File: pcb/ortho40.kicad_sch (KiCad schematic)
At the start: 129 parts, among them J1 SWD, J2 USB_C_Receptacle_USB2.0, SW1 SW_Push, U1 RP2040, U2 XC6206PxxxMR, U3 W25Q128JVS, U4 USBLC6-2SC6, U5 ST7735S_1.8inch, Y1 12MHz

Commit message: Fully finish PCB
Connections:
- net c0: now also U1.34 (GPIO22)
- net c1: now also U1.35 (GPIO23)
- net c10: now also U1.6 (GPIO4)
- net c11: now also U1.7 (GPIO5)
- net c2: now also U1.36 (GPIO24)
- net c3: now also U1.37 (GPIO25)
- net c4: now also U1.38 (GPIO26/ADC0)
- net c5: now also U1.39 (GPIO27/ADC1)
- net c6: now also U1.2 (GPIO0)
- net c7: now also U1.3 (GPIO1)
- net c8: now also U1.4 (GPIO2)
- net c9: now also U1.5 (GPIO3)
- net r0: now also U1.41 (GPIO29/ADC3)
- net r1: now also U1.40 (GPIO28/ADC2)
- net r2: now also U1.13 (GPIO10)
- net r3: now also U1.14 (GPIO11)
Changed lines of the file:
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@@
     (effects (font (size 1.27 1.27) italic) (justify left bottom))
   )
+  (global_label "c4" (shape input) (at 76.708 100.584 0) (fields_autoplaced)
+    (effects (font (size 1.27 1.27)) (justify left))
+    (property "Intersheet References" "${INTERSHEET_REFS}" (id 0) (at 81.4192 100.5046 0)
+      (effects (font (size 1.27 1.27)) (justify left) hide)
+    )
+  )
   (global_label "LCD_RESET" (shape input) (at 43.942 168.91 180) (fields_autoplaced)
     (effects (font (size 1.27 1.27)) (justify right))
@@
     )
   )
+  (global_label "c11" (shape input) (at 76.708 43.434 0) (fields_autoplaced)
+    (effects (font (size 1.27 1.27)) (justify left))
+    (property "Intersheet References" "${INTERSHEET_REFS}" (id 0) (at 82.6287 43.3546 0)
+      (effects (font (size 1.27 1.27)) (justify left) hide)
+    )
+  )
   (global_label "USB_DP" (shape input) (at 258.826 131.572 0) (fields_autoplaced)
     (effects (font (size 1.27 1.27)) (justify left))
@@
     )
   )
+  (global_label "c2" (shape input) (at 76.708 91.694 0) (fields_autoplaced)
+    (effects (font (size 1.27 1.27)) (justify left))
+    (property "Intersheet References" "${INTERSHEET_REFS}" (id 0) (at 81.4192 91.6146 0)
+      (effects (font (size 1.27 1.27)) (justify left) hide)
+    )
+  )
   (global_label "SWCLK" (shape input) (at 86.868 27.94 0) (fields_autoplaced)
     (effects (font (size 1.27 1.27)) (justify left))
@@
     )
   )
+  (global_label "r2" (shape input) (at 76.708 56.134 0) (fields_autoplaced)
+    (effects (font (size 1.27 1.27)) (justify left))
+    (property "Intersheet References" "${INTERSHEET_REFS}" (id 0) (at 81.1168 56.0546 0)
+      (effects (font (size 1.27 1.27)) (justify left) hide)
+    )
+  )
   (global_label "DN" (shape input) (at 220.98 148.336 0) (fields_autoplaced)
     (effects (font (size 1.27 1.27)) (justify left))
@@
     )
   )
+  (global_label "c7" (shape input) (at 76.708 33.274 0) (fields_autoplaced)
+    (effects (font (size 1.27 1.27)) (justify left))
+    (property "Intersheet References" "${INTERSHEET_REFS}" (id 0) (at 81.4192 33.1946 0)
+      (effects (font (size 1.27 1.27)) (justify left) hide)
+    )
+  )
   (global_label "CLK_OUT" (shape input) (at 178.816 152.908 0) (fields_autoplaced)
     (effects (font (size 1.27 1.27)) (justify left))
@@
     )
   )
+  (global_label "c6" (shape input) (at 76.708 30.734 0) (fields_autoplaced)
+    (effects (font (size 1.27 1.27)) (justify left))
+    (property "Intersheet References" "${INTERSHEET_REFS}" (id 0) (at 81.4192 30.6546 0)
+      (effects (font (size 1.27 1.27)) (justify left) hide)
+    )
+  )
   (global_label "c9" (shape input) (at 224.79 19.558 90) (fields_autoplaced)
     (effects (font (size 1.27 1.27)) (justify left))
@@
     )
   )
+  (global_label "r1" (shape input) (at 76.708 105.664 0) (fields_autoplaced)
+    (effects (font (size 1.27 1.27)) (justify left))
+    (property "Intersheet References" "${INTERSHEET_REFS}" (id 0) (at 81.1168 105.5846 0)
+      (effects (font (size 1.27 1.27)) (justify left) hide)
+    )
+  )
   (global_label "LCD_DC" (shape input) (at 43.942 171.45 180) (fields_autoplaced)
     (effects (font (size 1.27 1.27)) (justify right))
@@
     )
   )
+  (global_label "c0" (shape input) (at 76.708 86.614 0) (fields_autoplaced)
+    (effects (font (size 1.27 1.27)) (justify left))
+    (property "Intersheet References" "${INTERSHEET_REFS}" (id 0) (at 81.4192 86.5346 0)
+      (effects (font (size 1.27 1.27)) (justify left) hide)
+    )
+  )
   (global_label "QSPI_SD2" (shape input) (at 179.578 128.524 0) (fields_autoplaced)
     (effects (font (size 1.27 1.27)) (justify left))
@@
     )
   )
+  (global_label "c1" (shape input) (at 76.708 89.154 0) (fields_autoplaced)
+    (effects (font (size 1.27 1.27)) (justify left))
+    (property "Intersheet References" "${INTERSHEET_REFS}" (id 0) (at 81.4192 89.0746 0)
+      (effects (font (size 1.27 1.27)) (justify left) hide)
+    )
+  )
   (global_label "CLK_IN" (shape input) (at 178.816 147.828 0) (fields_autoplaced)
     (effects (font (size 1.27 1.27)) (justify left))
@@
     )
   )
+  (global_label "c8" (shape input) (at 76.708 35.814 0) (fields_autoplaced)
+    (effects (font (size 1.27 1.27)) (justify left))
+    (property "Intersheet References" "${INTERSHEET_REFS}" (id 0) (at 81.4192 35.7346 0)
+      (effects (font (size 1.27 1.27)) (justify left) hide)
+    )
+  )
   (global_label "c4" (shape input) (at 161.29 19.304 90) (fields_autoplaced)
     (effects (font (size 1.27 1.27)) (justify left))
@@
     )
   )
+  (global_label "r3" (shape input) (at 76.708 58.674 0) (fields_autoplaced)
+    (effects (font (size 1.27 1.27)) (justify left))
+    (property "Intersheet References" "${INTERSHEET_REFS}" (id 0) (at 81.1168 58.5946 0)
+      (effects (font (size 1.27 1.27)) (justify left) hide)
+    )
+  )
   (global_label "QSPI_SCLK" (shape input) (at 154.178 128.524 180) (fields_autoplaced)
     (effects (font (size 1.27 1.27)) (justify right))
@@
     )
   )
+  (global_label "c3" (shape input) (at 76.708 94.234 0) (fields_autoplaced)
+    (effects (font (size 1.27 1.27)) (justify left))
+    (property "Intersheet References" "${INTERSHEET_REFS}" (id 0) (at 81.4192 94.1546 0)
+      (effects (font (size 1.27 1.27)) (justify left) hide)
+    )
+  )
   (global_label "r1" (shape input) (at 93.726 57.912 180) (fields_autoplaced)
     (effects (font (size 1.27 1.27)) (justify right))
@@
     )
   )
+  (global_label "r0" (shape input) (at 76.708 108.204 0) (fields_autoplaced)
+    (effects (font (size 1.27 1.27)) (justify left))
+    (property "Intersheet References" "${INTERSHEET_REFS}" (id 0) (at 81.1168 108.1246 0)
+      (effects (font (size 1.27 1.27)) (justify left) hide)
+    )
+  )
   (global_label "QSPI_SD0" (shape input) (at 36.068 98.044 180) (fields_autoplaced)
     (effects (font (size 1.27 1.27)) (justify right))
@@
     )
   )
+  (global_label "c5" (shape input) (at 76.708 103.124 0) (fields_autoplaced)
+    (effects (font (size 1.27 1.27)) (justify left))
+    (property "Intersheet References" "${INTERSHEET_REFS}" (id 0) (at 81.4192 103.0446 0)
+      (effects (font (size 1.27 1.27)) (justify left) hide)
+    )
+  )
   (global_label "SWCLK" (shape input) (at 36.068 85.344 180) (fields_autoplaced)
     (effects (font (size 1.27 1.27)) (justify right))
@@
     )
   )
+  (global_label "c9" (shape input) (at 76.708 38.354 0) (fields_autoplaced)
+    (effects (font (size 1.27 1.27)) (justify left))
+    (property "Intersheet References" "${INTERSHEET_REFS}" (id 0) (at 81.4192 38.2746 0)
+      (effects (font (size 1.27 1.27)) (justify left) hide)
+    )
+  )
   (global_label "c1" (shape input) (at 123.19 19.304 90) (fields_autoplaced)
     (effects (font (size 1.27 1.27)) (justify left))
@@
     (property "Intersheet References" "${INTERSHEET_REFS}" (id 0) (at 34.816 161.2106 0)
       (effects (font (size 1.27 1.27)) (justify right) hide)
+    )
+  )
+  (global_label "c10" (shape input) (at 76.708 40.894 0) (fields_autoplaced)
+    (effects (font (size 1.27 1.27)) (justify left))
+    (property "Intersheet References" "${INTERSHEET_REFS}" (id 0) (at 82.6287 40.8146 0)
+      (effects (font (size 1.27 1.27)) (justify left) hide)
     )
   )
@@
     )
     (pin "1")
+    (pin "10")
     (pin "2")
     (pin "3")
@@
     (pin "8")
     (pin "9")
-    (pin "10")
   )
   (symbol (lib_id "Device:R_Small") (at 149.098 123.444 90) (unit 1)

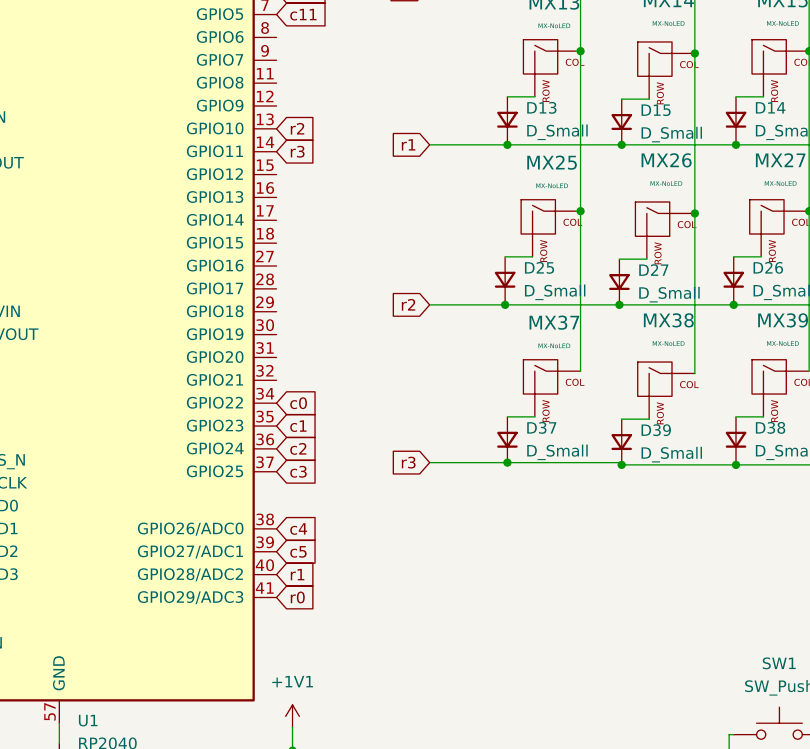
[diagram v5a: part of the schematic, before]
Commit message: Setup Display
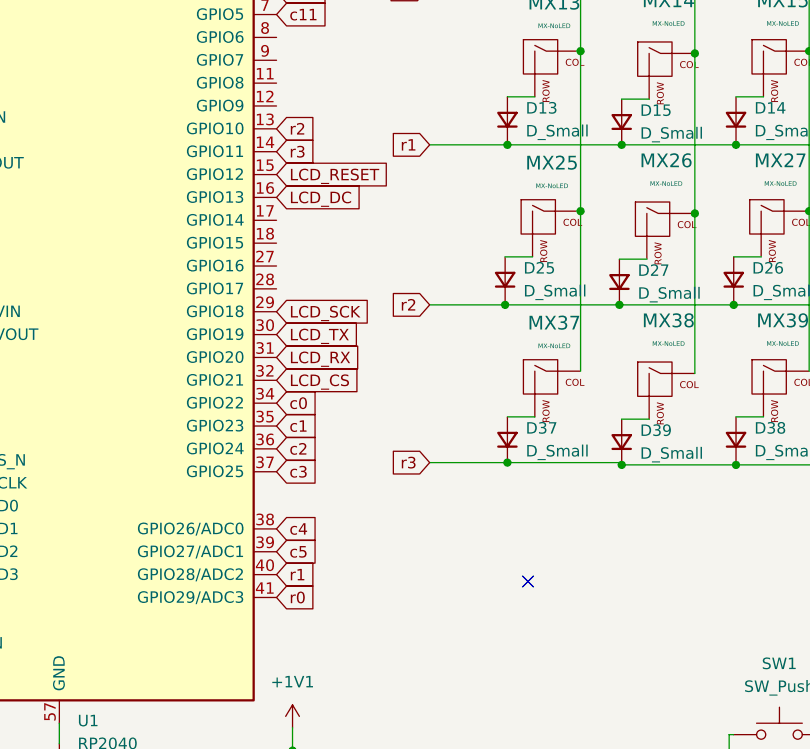
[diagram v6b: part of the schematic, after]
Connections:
- net LCD_CS: now also U1.32 (GPIO21)
- net LCD_DC: now also U1.16 (GPIO13)
- net LCD_RESET: now also U1.15 (GPIO12)
- net LCD_RX: now also U1.31 (GPIO20)
- net LCD_SCK: now also U1.29 (GPIO18)
- net LCD_TX: now also U1.30 (GPIO19)
- no-connect marks 2 -> 3
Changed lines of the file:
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@@
   (no_connect (at 258.826 140.462))
   (no_connect (at 258.826 143.002))
+  (no_connect (at 104.648 106.426))
   (wire (pts (xy 203.2 106.68) (xy 203.2 108.712))
     (stroke (width 0) (type default) (color 0 0 0 0))
@@
     (effects (font (size 1.27 1.27) italic) (justify left bottom))
   )
+  (global_label "LCD_SCK" (shape input) (at 76.708 76.454 0) (fields_autoplaced)
+    (effects (font (size 1.27 1.27)) (justify left))
+    (property "Intersheet References" "${INTERSHEET_REFS}" (id 0) (at 87.4063 76.3746 0)
+      (effects (font (size 1.27 1.27)) (justify left) hide)
+    )
+  )
   (global_label "c4" (shape input) (at 76.708 100.584 0) (fields_autoplaced)
     (effects (font (size 1.27 1.27)) (justify left))
@@
     )
   )
+  (global_label "LCD_RESET" (shape input) (at 76.708 61.214 0) (fields_autoplaced)
+    (effects (font (size 1.27 1.27)) (justify left))
+    (property "Intersheet References" "${INTERSHEET_REFS}" (id 0) (at 89.4021 61.1346 0)
+      (effects (font (size 1.27 1.27)) (justify left) hide)
+    )
+  )
   (global_label "SWD" (shape input) (at 36.068 87.884 180) (fields_autoplaced)
     (effects (font (size 1.27 1.27)) (justify right))
@@
     )
   )
+  (global_label "LCD_TX" (shape input) (at 76.708 78.994 0) (fields_autoplaced)
+    (effects (font (size 1.27 1.27)) (justify left))
+    (property "Intersheet References" "${INTERSHEET_REFS}" (id 0) (at 85.834 78.9146 0)
+      (effects (font (size 1.27 1.27)) (justify left) hide)
+    )
+  )
   (global_label "c0" (shape input) (at 76.708 86.614 0) (fields_autoplaced)
     (effects (font (size 1.27 1.27)) (justify left))
@@
     )
   )
+  (global_label "LCD_CS" (shape input) (at 76.708 84.074 0) (fields_autoplaced)
+    (effects (font (size 1.27 1.27)) (justify left))
+    (property "Intersheet References" "${INTERSHEET_REFS}" (id 0) (at 86.1363 83.9946 0)
+      (effects (font (size 1.27 1.27)) (justify left) hide)
+    )
+  )
   (global_label "QSPI_SD2" (shape input) (at 179.578 128.524 0) (fields_autoplaced)
     (effects (font (size 1.27 1.27)) (justify left))
@@
     )
   )
+  (global_label "LCD_RX" (shape input) (at 76.708 81.534 0) (fields_autoplaced)
+    (effects (font (size 1.27 1.27)) (justify left))
+    (property "Intersheet References" "${INTERSHEET_REFS}" (id 0) (at 86.1363 81.4546 0)
+      (effects (font (size 1.27 1.27)) (justify left) hide)
+    )
+  )
   (global_label "r0" (shape input) (at 93.472 40.64 180) (fields_autoplaced)
     (effects (font (size 1.27 1.27)) (justify right))
@@
     )
   )
+  (global_label "LCD_DC" (shape input) (at 76.708 63.754 0) (fields_autoplaced)
+    (effects (font (size 1.27 1.27)) (justify left))
+    (property "Intersheet References" "${INTERSHEET_REFS}" (id 0) (at 86.1968 63.6746 0)
+      (effects (font (size 1.27 1.27)) (justify left) hide)
+    )
+  )

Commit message: Updates...
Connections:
- net LCD_BACKLT: now also U1.18 (GPIO15)
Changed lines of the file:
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@@
+    )
+  )
+  (global_label "LCD_BACKLT" (shape input) (at 76.708 68.834 0) (fields_autoplaced)
+    (effects (font (size 1.27 1.27)) (justify left))
+    (property "Intersheet References" "${INTERSHEET_REFS}" (id 0) (at 90.5511 68.7546 0)
+      (effects (font (size 1.27 1.27)) (justify left) hide)
     )
   )
